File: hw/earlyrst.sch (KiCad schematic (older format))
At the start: 4 parts, among them U201 74HC393, U202 74HC32, U203 74HC175, U204 74HC541

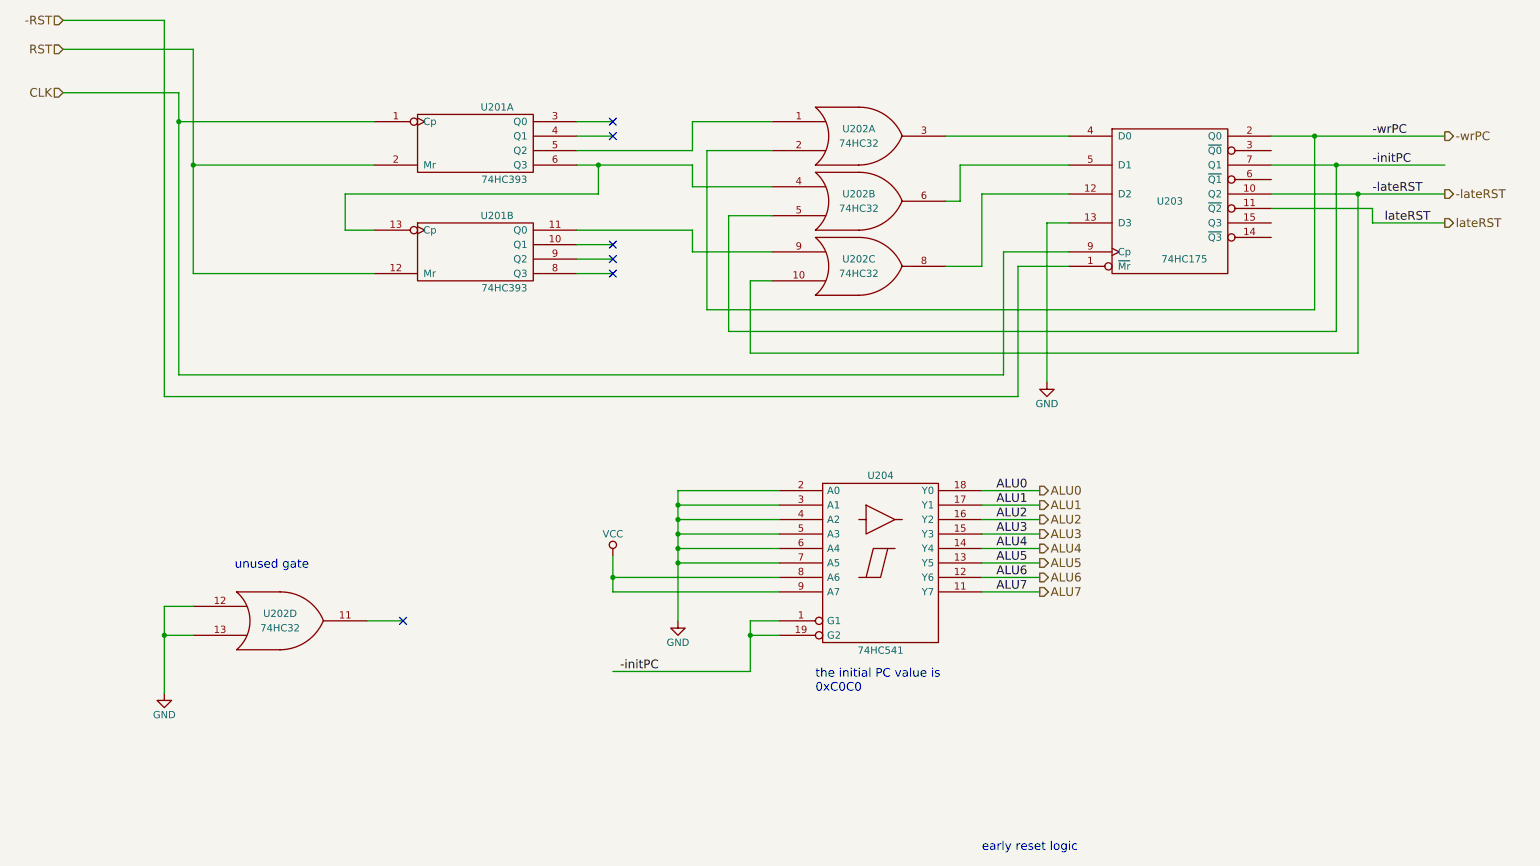
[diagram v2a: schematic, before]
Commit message: buffer clock/reset signals in earlyrst module
This is the place that makes sense because the late
reset signal is the one that matters to the rest
of the circuit.
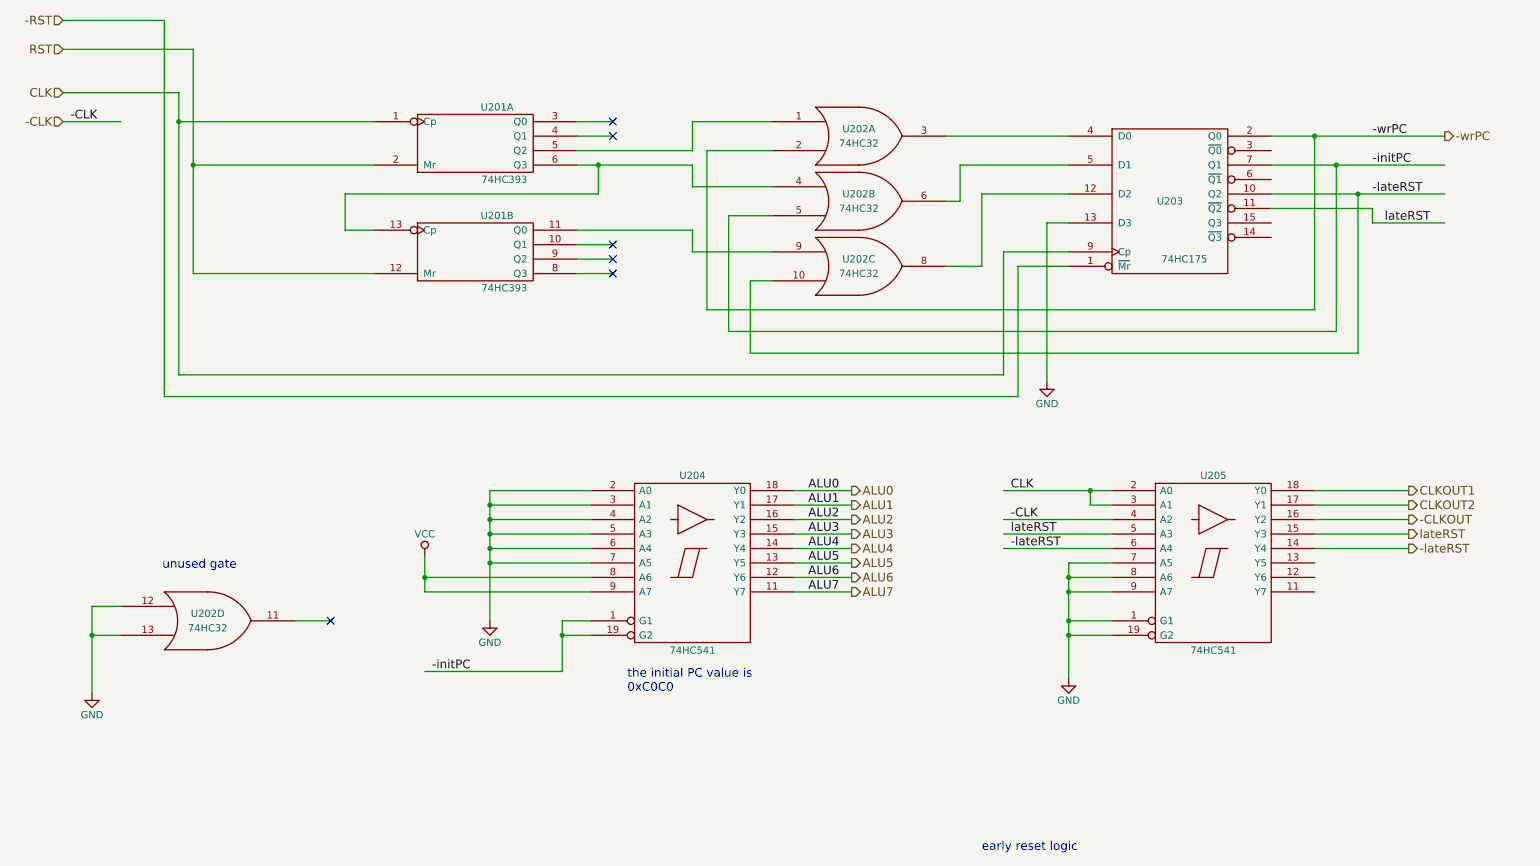
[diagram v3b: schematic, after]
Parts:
- added U205: 74HC541, symbol 74LS541
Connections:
- net labels added: -CLK, -CLKOUT, CLKOUT1, CLKOUT2
- wire segments 86 -> 104
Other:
- moved on the sheet: U202D, U204

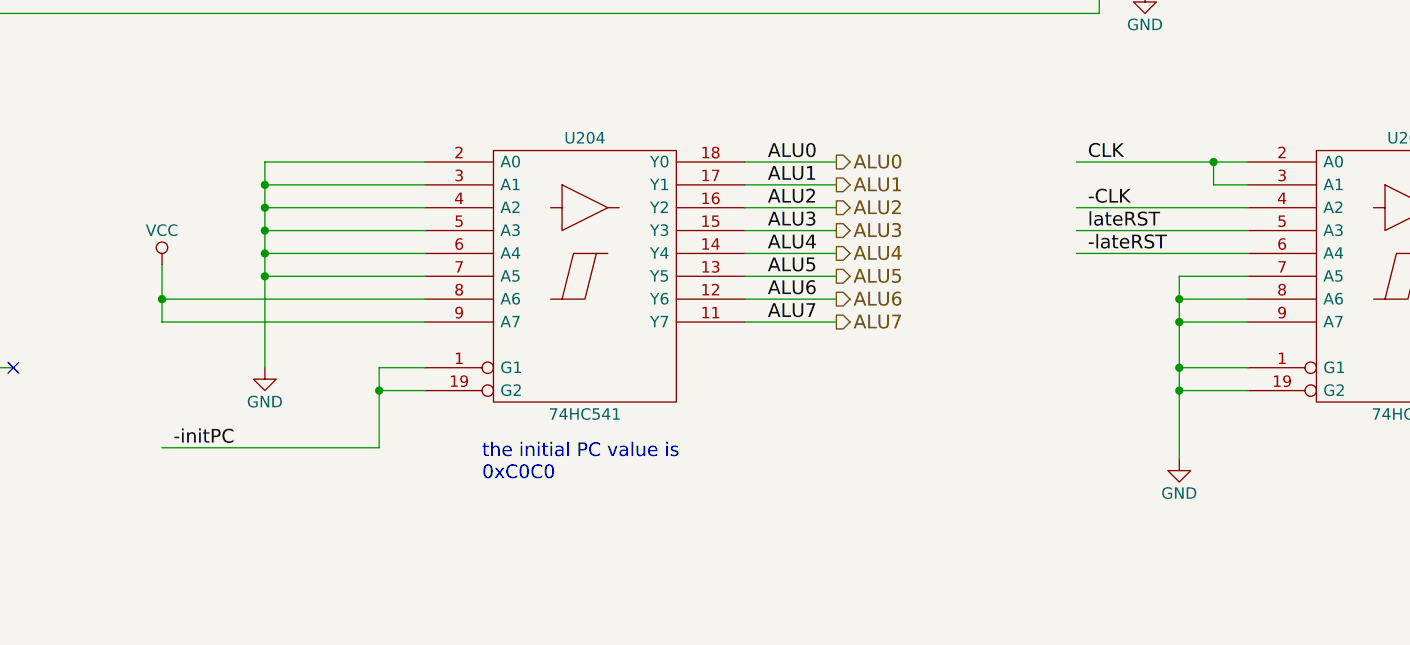
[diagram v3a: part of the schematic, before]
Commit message: simplified control of initial PC output
Just tie one of the '541 buffer's output enables to
ground, and control the other one using the -initPC
signal.
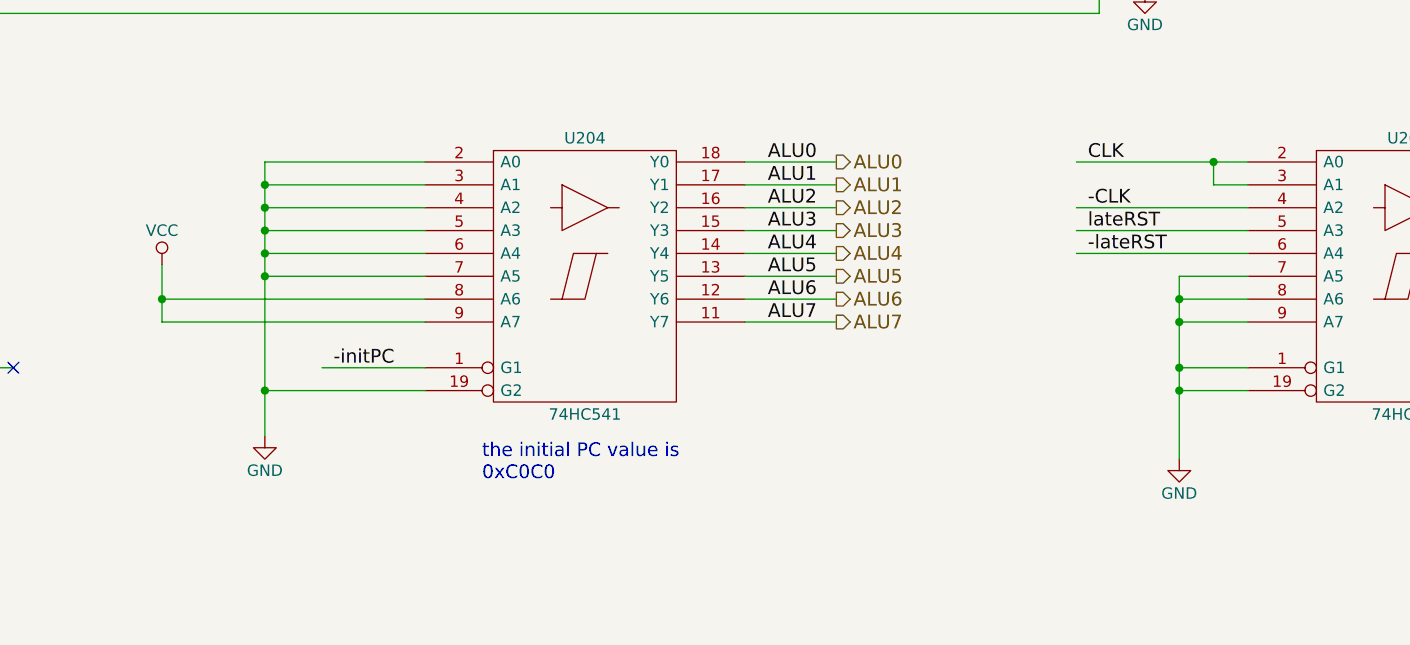
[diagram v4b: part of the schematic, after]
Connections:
- wire segments 104 -> 102
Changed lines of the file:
@@
 L GND #PWR?
 U 1 1 592B63DA
-P 3900 5200
-F 0 "#PWR?" H 3900 4950 50  0001 C CNN
-F 1 "GND" H 3900 5050 50  0000 C CNN
-F 2 "" H 3900 5200 50  0001 C CNN
-F 3 "" H 3900 5200 50  0001 C CNN
-	1    3900 5200
+P 3900 5500
+F 0 "#PWR?" H 3900 5250 50  0001 C CNN
+F 1 "GND" H 3900 5350 50  0000 C CNN
+F 2 "" H 3900 5500 50  0001 C CNN
+F 3 "" H 3900 5500 50  0001 C CNN
+	1    3900 5500
 	1    0    0    -1
 $EndComp
@@
 Text Label 10000 2250 0    60   ~ 0
 -lateRST
-Text Label 3500 5550 0    60   ~ 0
+Text Label 4200 5200 0    60   ~ 0
 -initPC
 $Comp
@@
 	4600 4300 3900 4300
 Wire Wire Line
-	3900 4300 3900 5200
+	3900 4300 3900 5500
 Wire Wire Line
 	4600 4400 3900 4400
@@
 	7550 2750 7900 2750
 Wire Wire Line
-	4600 5200 4400 5200
-Wire Wire Line
-	4400 5200 4400 5550
-Wire Wire Line
-	4400 5550 3450 5550
-Wire Wire Line
-	4600 5300 4400 5300
-Connection ~ 4400 5300
+	4600 5200 4150 5200
+Wire Wire Line
+	3900 5300 4600 5300
 Wire Wire Line
 	1350 5100 1150 5100
@@
 $EndComp
 Wire Wire Line
-	8200 4300 7450 4300
+	7450 4300 8200 4300
 Wire Wire Line
 	8200 4400 8050 4400
@@
 Text HLabel 10250 4700 2    60   Output ~ 0
 -lateRST
+Connection ~ 3900 5300
 $EndSCHEMATC
